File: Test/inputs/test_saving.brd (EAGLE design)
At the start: 160 x 100 mm, 9 parts

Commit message: Major improvements to bounding boxes. Now supports: arcs (with width), long pads, offset pads, rotated offset/long pads, rotated octagons. With tests.
git-svn-id: svn+ssh://bbfs-01.calit2.net/grw/Gordon/svn/trunk/Gadgets/Tools/CircuitsByCode@20711 2cf53259-273a-af40-bda6-69d31023b8ec
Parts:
- added TEST-ARC3: TEST-ARC3, Swoop-Test-Packages:TEST-ARC3
- added TEST-PAD-OCT: TEST-PAD-OCT, Swoop-Test-Packages:TEST-PAD-OCT
- added TEST-PAD-OCT2: TEST-PAD-OCT2, Swoop-Test-Packages:TEST-PAD-OCT2
- added TEST-PAD-ROT: TEST-PAD-ROT, Swoop-Test-Packages:TEST-PAD-ROT
- added TEST-PAD-SQUARE-ROT: TEST-PAD-SQUARE-ROT, Swoop-Test-Packages:TEST-PAD-SQUARE-ROT
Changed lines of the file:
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@@
 <element name="TEST-PAD-SQUARE" library="Swoop-Test-Packages" package="TEST-PAD3" value="TEST-PAD3" x="119" y="74"/>
 <element name="TEST-PAD-ROUND" library="Swoop-Test-Packages" package="TEST-PAD-ROUND" value="TEST-PAD-ROUND" x="131" y="76"/>
+<element name="TEST-ARC3" library="Swoop-Test-Packages" package="TEST-ARC3" value="TEST-ARC3" x="139" y="88"/>
+<element name="TEST-PAD-ROT" library="Swoop-Test-Packages" package="TEST-PAD-ROT" value="TEST-PAD-ROT" x="138" y="79"/>
+<element name="TEST-PAD-OCT" library="Swoop-Test-Packages" package="TEST-PAD-OCT" value="TEST-PAD-OCT" x="114" y="70"/>
+<element name="TEST-PAD-SQUARE-ROT" library="Swoop-Test-Packages" package="TEST-PAD-SQUARE-ROT" value="TEST-PAD-SQUARE-ROT" x="118" y="82"/>
+<element name="TEST-PAD-OCT2" library="Swoop-Test-Packages" package="TEST-PAD-OCT2" value="TEST-PAD-OCT2" x="126" y="72"/>
 </elements>
 <signals>

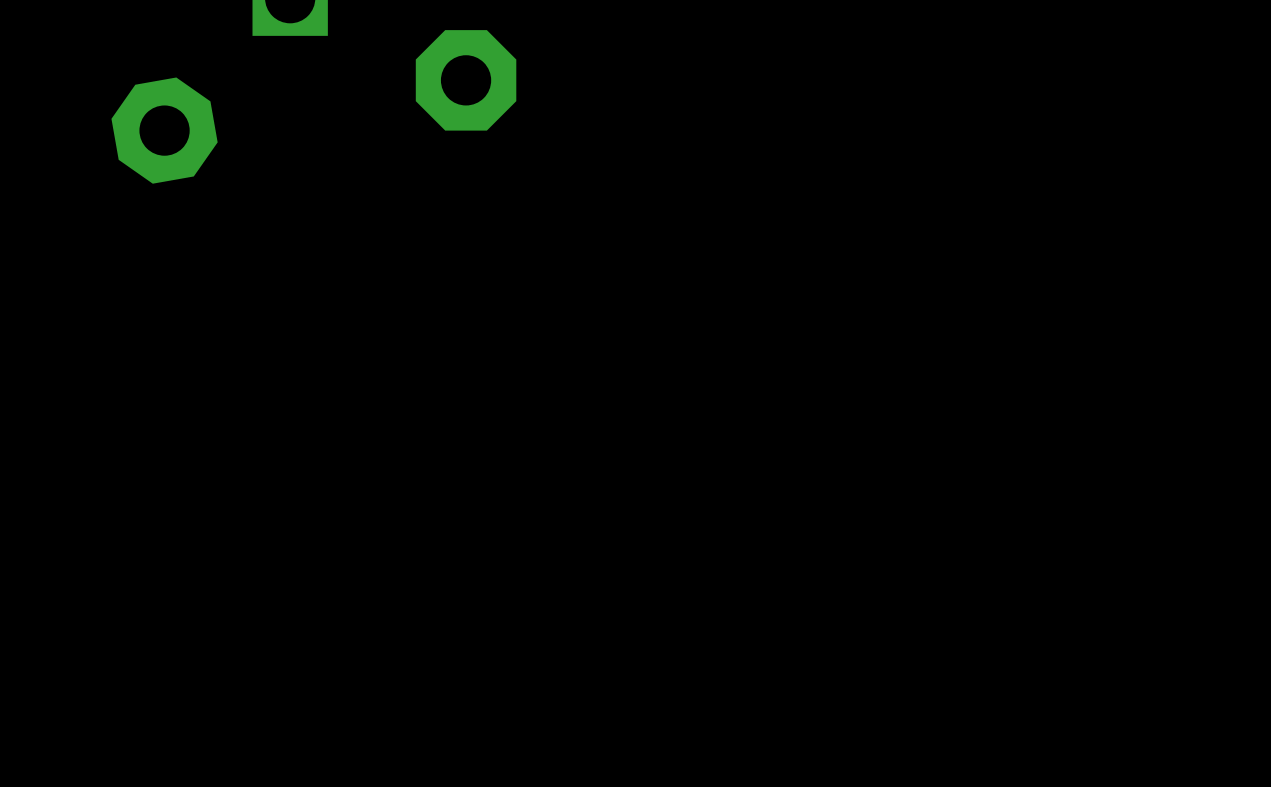
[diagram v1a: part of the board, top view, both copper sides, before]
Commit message: Added holes and circles
git-svn-id: svn+ssh://bbfs-01.calit2.net/grw/Gordon/svn/trunk/Gadgets/Tools/CircuitsByCode@20788 2cf53259-273a-af40-bda6-69d31023b8ec
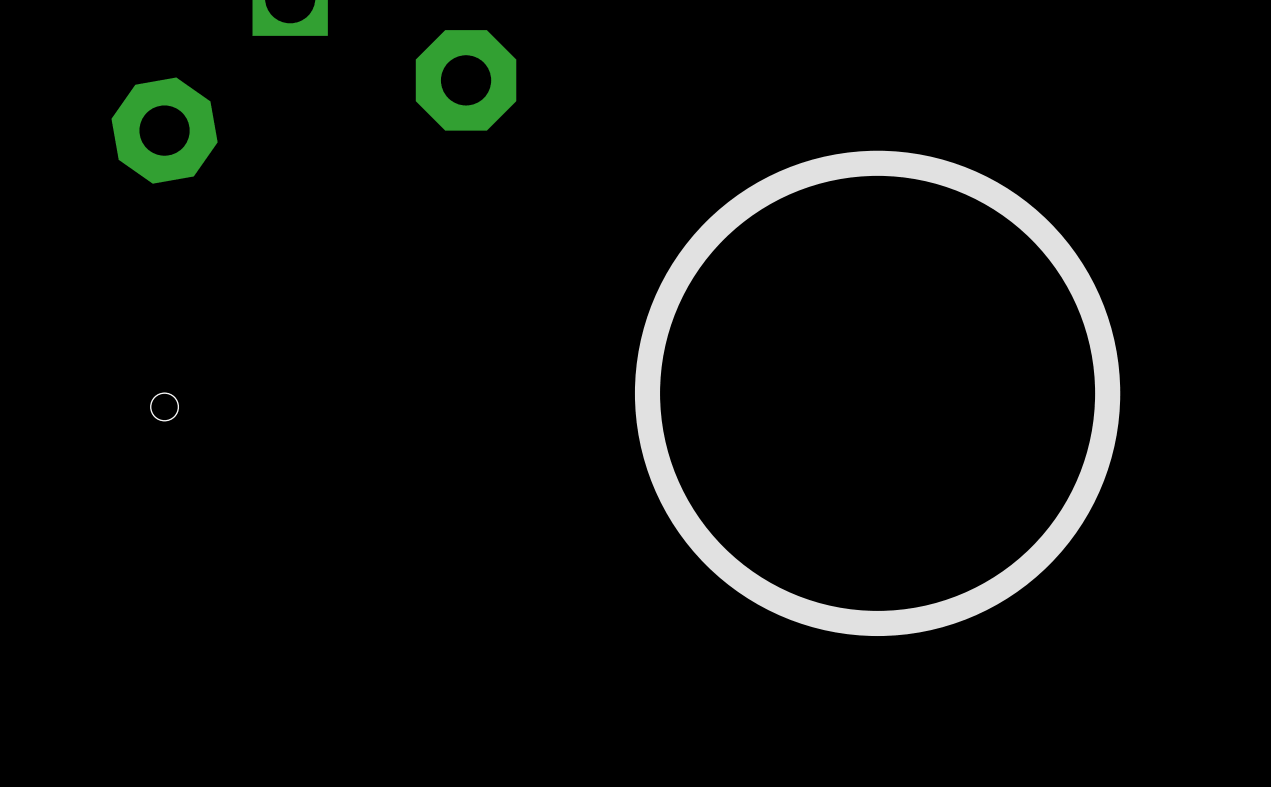
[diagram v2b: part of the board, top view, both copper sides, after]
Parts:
- added TEST-CIRCLE: TEST-CIRCLE, Swoop-Test-Packages:TEST-CIRCLE
- added TEST-HOLE: TEST-HOLE, Swoop-Test-Packages:TEST-HOLE
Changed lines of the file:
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@@
 <element name="TEST-PAD-SQUARE-ROT" library="Swoop-Test-Packages" package="TEST-PAD-SQUARE-ROT" value="TEST-PAD-SQUARE-ROT" x="118" y="82"/>
 <element name="TEST-PAD-OCT2" library="Swoop-Test-Packages" package="TEST-PAD-OCT2" value="TEST-PAD-OCT2" x="126" y="72"/>
+<element name="TEST-CIRCLE" library="Swoop-Test-Packages" package="TEST-CIRCLE" value="TEST-CIRCLE" x="150" y="57"/>
+<element name="TEST-HOLE" library="Swoop-Test-Packages" package="TEST-HOLE" value="TEST-HOLE" x="115" y="58"/>
 </elements>
 <signals>
